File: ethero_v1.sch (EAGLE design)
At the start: 20 parts, among them IC1 ENC28J60SP, X1 GLX-S-88M

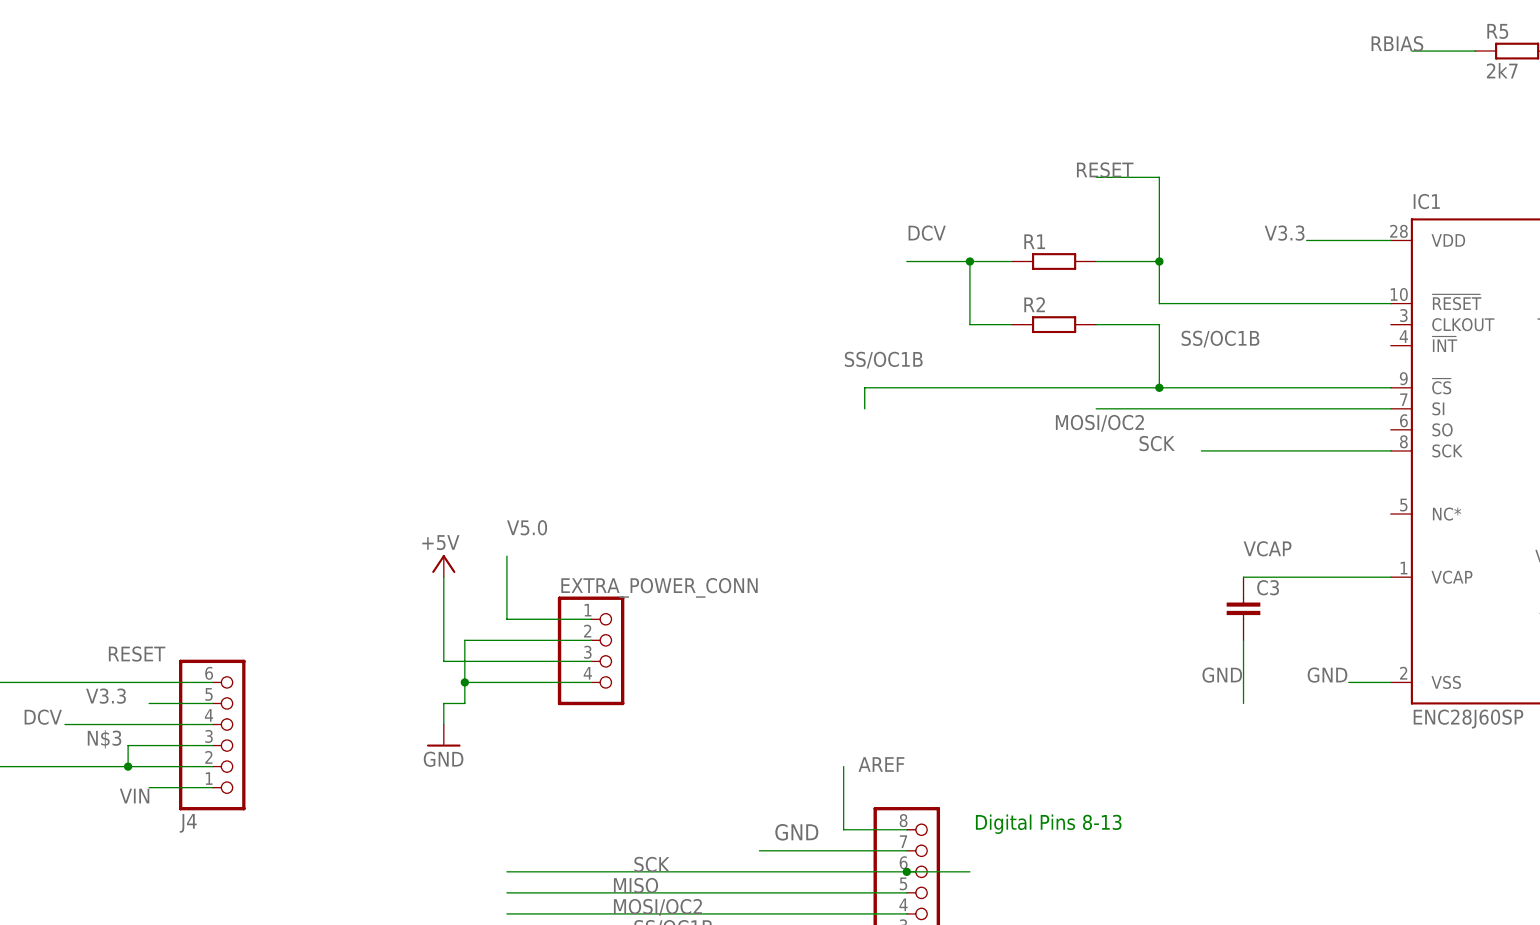
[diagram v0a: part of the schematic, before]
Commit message: added non inverting buffer for level switching
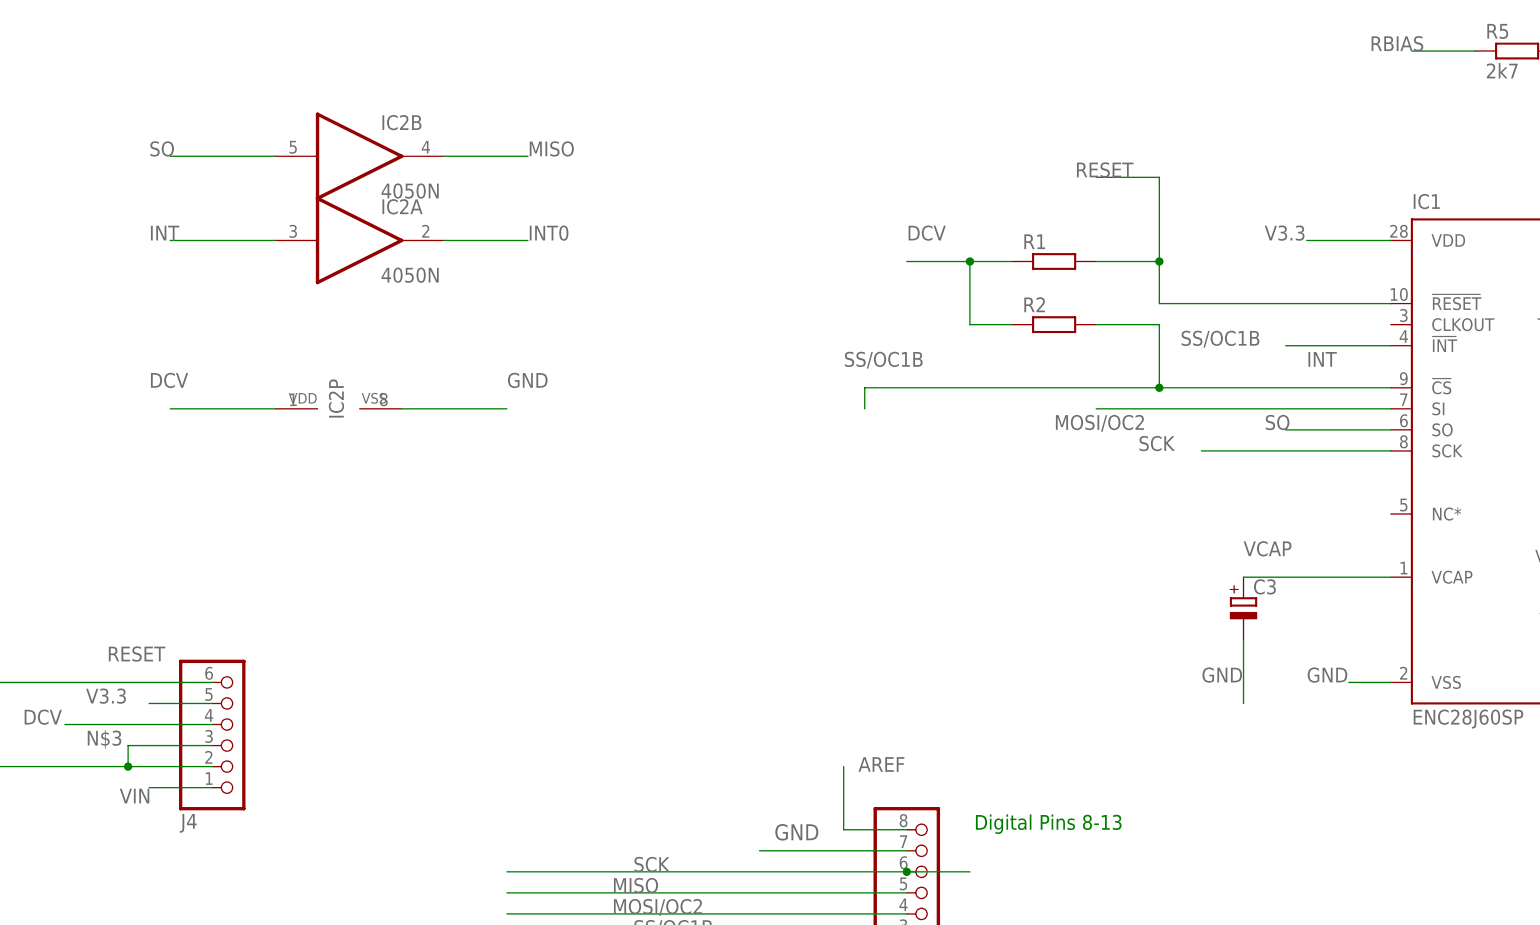
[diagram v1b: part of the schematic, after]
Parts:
- removed EXTRA_POWER_CONN: (no value), pinhead:PINHD-1X4
- added IC2: 4050N, 40xx:4050N
- C3: device resistor:C-EU025-025X050 -> rcl:CPOL-EUE5-5
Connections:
- removed net V5.0: EXTRA_POWER_CONN.1
- new net INT: IC1.!INT, IC2A.I
- new net SO: IC1.SO, IC2B.I
- net DCV: now also IC2P.VDD; no longer EXTRA_POWER_CONN.3
- net GND: now also C3.-, IC2P.VSS; no longer C3.2, EXTRA_POWER_CONN.2, EXTRA_POWER_CONN.4
- net INT0: now also IC2A.O
- net MISO: now also IC2B.O
- net VCAP: now also C3.+; no longer C3.1
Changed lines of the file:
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@@
 <part name="J4" library="pinhead" deviceset="PINHD-1X6" device=""/>
 <part name="GND2" library="supply1" deviceset="GND" device=""/>
-<part name="EXTRA_POWER_CONN" library="pinhead" deviceset="PINHD-1X4" device=""/>
-<part name="P+5" library="supply1" deviceset="+5V" device=""/>
-<part name="GND5" library="supply1" deviceset="GND" device=""/>
 <part name="IC1" library="microchip" deviceset="ENC28J60" device="SP"/>
 <part name="C1" library="resistor" deviceset="C-EU" device="025-025X050"/>
 <part name="C2" library="resistor" deviceset="C-EU" device="025-025X050"/>
-<part name="C3" library="resistor" deviceset="C-EU" device="025-025X050"/>
+<part name="C3" library="rcl" deviceset="CPOL-EU" device="E5-5"/>
 <part name="C4" library="resistor" deviceset="C-EU" device="025-025X050"/>
 <part name="C5" library="resistor" deviceset="C-EU" device="025-025X050"/>
@@
 <part name="GND6" library="supply1" deviceset="GND" device=""/>
 <part name="GND7" library="supply1" deviceset="GND" device=""/>
+<part name="IC2" library="40xx" deviceset="4050" device="N"/>
 </parts>
 <sheets>
@@
 <instance part="J4" gate="A" x="43.18" y="12.7" rot="MR180"/>
 <instance part="GND2" gate="1" x="160.02" y="-55.88"/>
-<instance part="EXTRA_POWER_CONN" gate="A" x="88.9" y="20.32"/>
-<instance part="P+5" gate="1" x="68.58" y="33.02" smashed="yes">
-<attribute name="VALUE" x="70.485" y="35.56" size="1.778" layer="96" rot="R180"/>
-</instance>
-<instance part="GND5" gate="1" x="68.58" y="10.16"/>
 <instance part="IC1" gate="G$1" x="198.12" y="45.72"/>
 <instance part="C1" gate="G$1" x="254" y="2.54"/>
@@
 <instance part="GND6" gate="1" x="205.74" y="88.9"/>
 <instance part="GND7" gate="1" x="279.4" y="50.8"/>
+<instance part="IC2" gate="A" x="58.42" y="71.12"/>
+<instance part="IC2" gate="B" x="58.42" y="81.28"/>
+<instance part="IC2" gate="P" x="55.88" y="50.8" rot="R90"/>
 </instances>
 <busses>
@@
 <wire x1="40.64" y1="12.7" x2="22.86" y2="12.7" width="0.1524" layer="91"/>
 <label x="17.78" y="12.7" size="1.778" layer="95"/>
-</segment>
-<segment>
-<pinref part="P+5" gate="1" pin="+5V"/>
-<pinref part="EXTRA_POWER_CONN" gate="A" pin="3"/>
-<wire x1="86.36" y1="20.32" x2="68.58" y2="20.32" width="0.1524" layer="91"/>
-<wire x1="68.58" y1="20.32" x2="68.58" y2="30.48" width="0.1524" layer="91"/>
 </segment>
 <segment>
@@
 <junction x="132.08" y="68.58"/>
 </segment>
+<segment>
+<pinref part="IC2" gate="P" pin="VDD"/>
+<wire x1="35.56" y1="50.8" x2="48.26" y2="50.8" width="0.1524" layer="91"/>
+<label x="33.02" y="53.34" size="1.778" layer="95"/>
+</segment>
 </net>
 <net name="GND" class="1">
@@
 <wire x1="-2.54" y1="-35.56" x2="-2.54" y2="-58.42" width="0.1524" layer="91"/>
 <pinref part="GND3" gate="1" pin="GND"/>
-</segment>
-<segment>
-<pinref part="EXTRA_POWER_CONN" gate="A" pin="2"/>
-<wire x1="86.36" y1="22.86" x2="71.12" y2="22.86" width="0.1524" layer="91"/>
-<wire x1="71.12" y1="22.86" x2="71.12" y2="17.78" width="0.1524" layer="91"/>
-<pinref part="GND5" gate="1" pin="GND"/>
-<wire x1="71.12" y1="17.78" x2="71.12" y2="15.24" width="0.1524" layer="91"/>
-<wire x1="71.12" y1="15.24" x2="68.58" y2="15.24" width="0.1524" layer="91"/>
-<wire x1="68.58" y1="15.24" x2="68.58" y2="12.7" width="0.1524" layer="91"/>
-<pinref part="EXTRA_POWER_CONN" gate="A" pin="4"/>
-<wire x1="86.36" y1="17.78" x2="71.12" y2="17.78" width="0.1524" layer="91"/>
-<junction x="71.12" y="17.78"/>
 </segment>
 <segment>
@@
 </segment>
 <segment>
-<pinref part="C3" gate="G$1" pin="2"/>
+<pinref part="C3" gate="G$1" pin="-"/>
 <wire x1="165.1" y1="22.86" x2="165.1" y2="15.24" width="0.1524" layer="91"/>
 <label x="160.02" y="17.78" size="1.778" layer="95"/>
+</segment>
+<segment>
+<pinref part="IC2" gate="P" pin="VSS"/>
+<wire x1="76.2" y1="50.8" x2="63.5" y2="50.8" width="0.1524" layer="91"/>
+<label x="76.2" y="53.34" size="1.778" layer="95"/>
 </segment>
 </net>
@@
 <wire x1="124.46" y1="-53.34" x2="76.2" y2="-53.34" width="0.1524" layer="91"/>
 <label x="91.44" y="-53.34" size="1.778" layer="95"/>
+</segment>
+<segment>
+<pinref part="IC2" gate="A" pin="O"/>
+<wire x1="78.74" y1="71.12" x2="68.58" y2="71.12" width="0.1524" layer="91"/>
+<label x="78.74" y="71.12" size="1.778" layer="95"/>
 </segment>
 </net>
@@
 <pinref part="J1" gate="A" pin="5"/>
 <label x="88.9" y="-7.62" size="1.778" layer="95"/>
+</segment>
+<segment>
+<pinref part="IC2" gate="B" pin="O"/>
+<wire x1="78.74" y1="81.28" x2="68.58" y2="81.28" width="0.1524" layer="91"/>
+<label x="78.74" y="81.28" size="1.778" layer="95"/>
 </segment>
 </net>
@@
 </segment>
 </net>
-<net name="V5.0" class="1">
-<segment>
-<pinref part="EXTRA_POWER_CONN" gate="A" pin="1"/>
-<wire x1="86.36" y1="25.4" x2="76.2" y2="25.4" width="0.1524" layer="91"/>
-<wire x1="76.2" y1="25.4" x2="76.2" y2="33.02" width="0.1524" layer="91"/>
-<label x="76.2" y="35.56" size="1.778" layer="95"/>
-</segment>
-</net>
 <net name="N$3" class="1">
 <segment>
@@
 <segment>
 <pinref part="IC1" gate="G$1" pin="VCAP"/>
-<pinref part="C3" gate="G$1" pin="1"/>
+<pinref part="C3" gate="G$1" pin="+"/>
 <wire x1="182.88" y1="30.48" x2="165.1" y2="30.48" width="0.1524" layer="91"/>
 <label x="165.1" y="33.02" size="1.778" layer="95"/>
 </segment>
 </net>
+<net name="SO" class="0">
+<segment>
+<pinref part="IC1" gate="G$1" pin="SO"/>
+<wire x1="170.18" y1="48.26" x2="182.88" y2="48.26" width="0.1524" layer="91"/>
+<label x="167.64" y="48.26" size="1.778" layer="95"/>
+</segment>
+<segment>
+<pinref part="IC2" gate="B" pin="I"/>
+<wire x1="35.56" y1="81.28" x2="48.26" y2="81.28" width="0.1524" layer="91"/>
+<label x="33.02" y="81.28" size="1.778" layer="95"/>
+</segment>
+</net>
+<net name="INT" class="0">
+<segment>
+<pinref part="IC1" gate="G$1" pin="!INT"/>
+<wire x1="170.18" y1="58.42" x2="182.88" y2="58.42" width="0.1524" layer="91"/>
+<label x="172.72" y="55.88" size="1.778" layer="95"/>
+</segment>
+<segment>
+<pinref part="IC2" gate="A" pin="I"/>
+<wire x1="35.56" y1="71.12" x2="48.26" y2="71.12" width="0.1524" layer="91"/>
+<label x="33.02" y="71.12" size="1.778" layer="95"/>
+</segment>
+</net>
